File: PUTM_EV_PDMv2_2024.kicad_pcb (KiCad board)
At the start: 4 copper layers, 60 x 40 mm, 4 parts

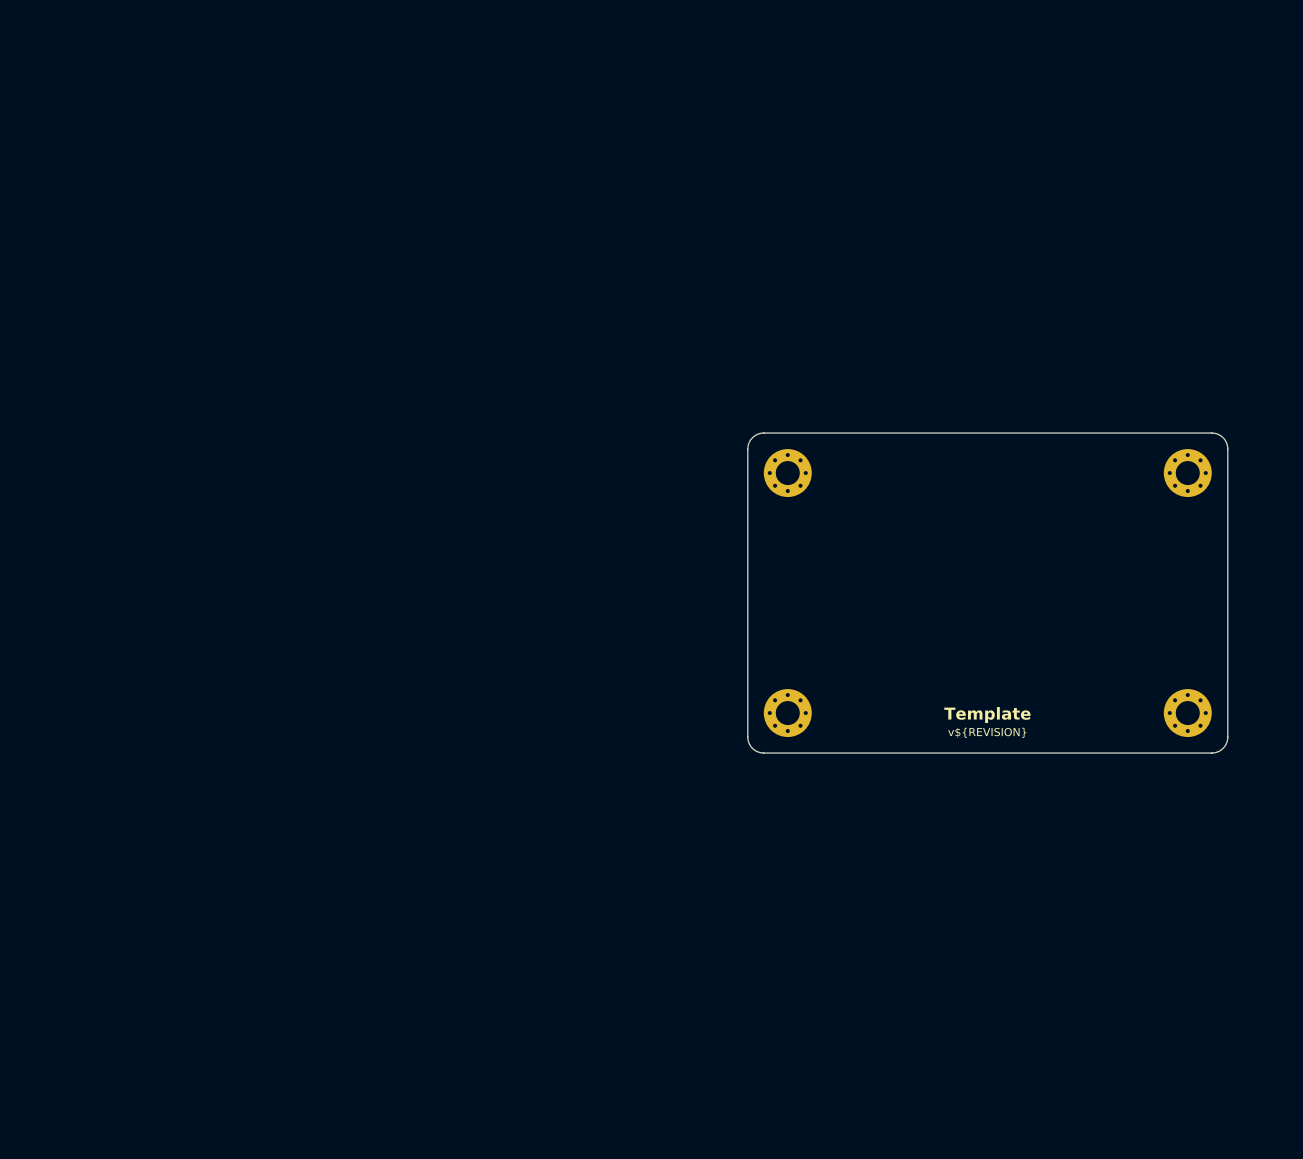
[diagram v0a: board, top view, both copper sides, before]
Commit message: Footprint changes + started PCB
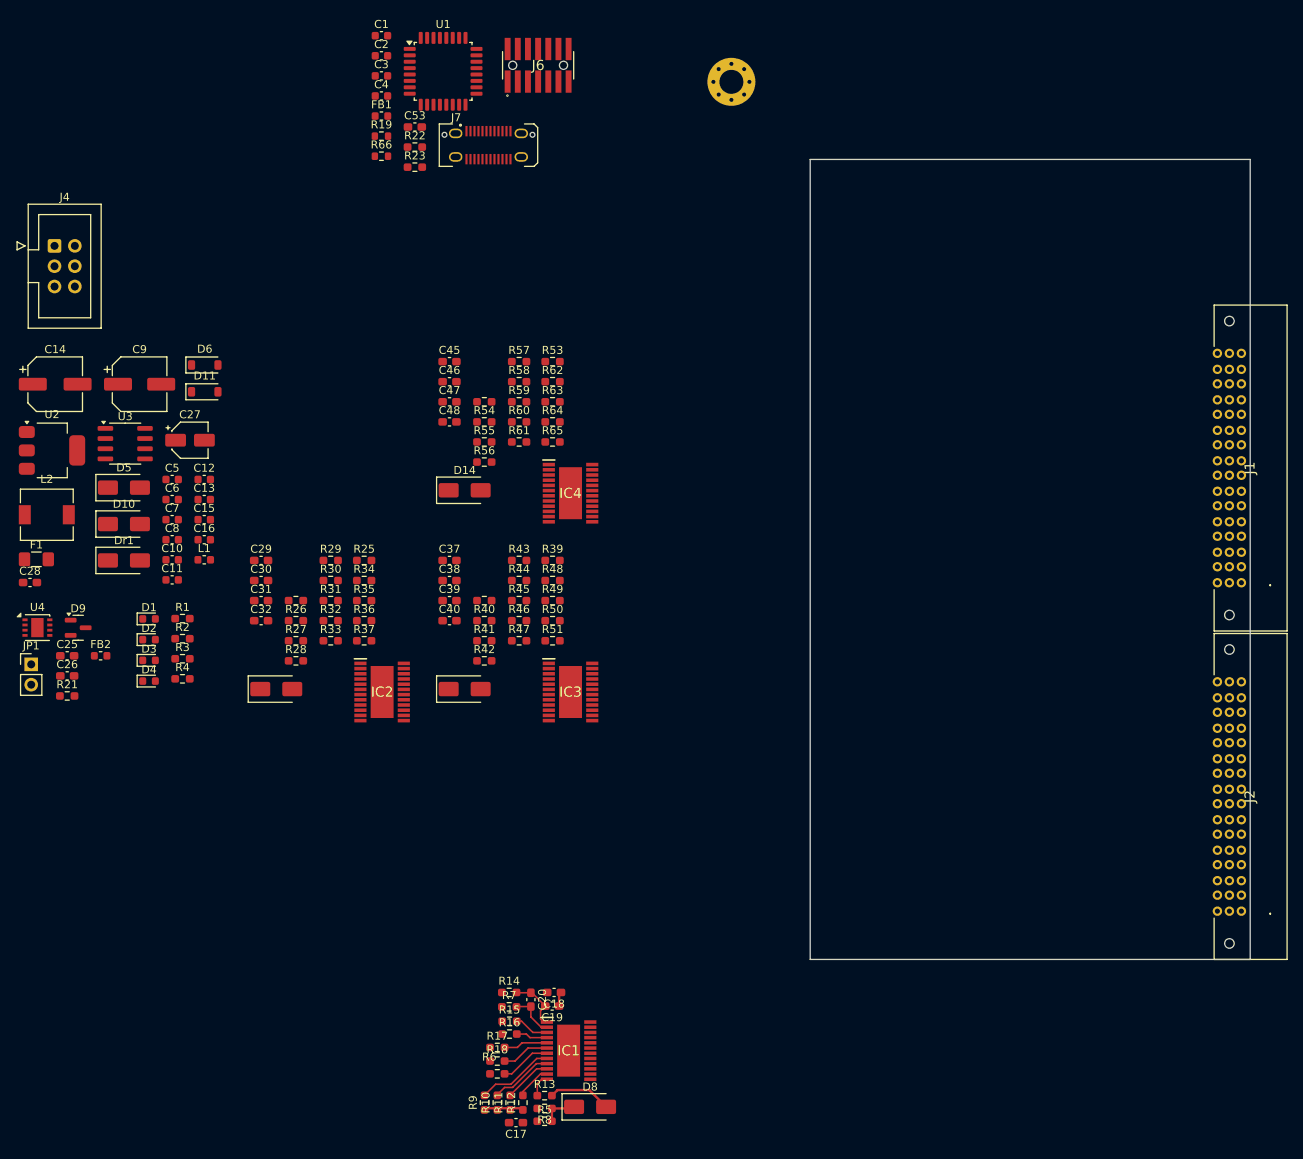
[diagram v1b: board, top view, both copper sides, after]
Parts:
- removed the REF** at (171.0, 81.0)
- removed the REF** at (121.0, 111.0)
- removed the REF** at (171.0, 111.0)
- added C1: 100n, Capacitor_SMD:C_0603_1608Metric, F.Cu at (70.2, 26.3)
- added C10: 100n, Capacitor_SMD:C_0603_1608Metric, F.Cu at (44.0, 91.8)
- added C11: 1u, Capacitor_SMD:C_0603_1608Metric, F.Cu at (44.0, 94.4)
- added C12: 10n, Capacitor_SMD:C_0603_1608Metric, F.Cu at (48.1, 81.8)
- added C13: 100n, Capacitor_SMD:C_0603_1608Metric, F.Cu at (48.1, 84.3)
- added C14: 68u, Capacitor_SMD:CP_Elec_6.3x5.4, F.Cu at (29.4, 69.9)
- added C15: 1u, Capacitor_SMD:C_0603_1608Metric, F.Cu at (48.1, 86.8)
- added C16: 100n, Capacitor_SMD:C_0603_1608Metric, F.Cu at (48.1, 89.3)
- added C17: 220p, Capacitor_SMD:C_0603_1608Metric_Pad1.08x0.95mm_HandSolder, F.Cu at (87.0, 162.2)
- added C18: 100n, Capacitor_SMD:C_0603_1608Metric_Pad1.08x0.95mm_HandSolder, F.Cu at (91.8, 145.9)
- added C19: 22n, Capacitor_SMD:C_0603_1608Metric_Pad1.08x0.95mm_HandSolder, F.Cu at (91.6, 147.6)
- added C2: 4.7u, Capacitor_SMD:C_0603_1608Metric, F.Cu at (70.2, 28.8)
- added C20: 470n, Capacitor_SMD:C_0603_1608Metric_Pad1.08x0.95mm_HandSolder, F.Cu at (88.9, 146.8)
- added C25: 100nF, Capacitor_SMD:C_0603_1608Metric_Pad1.08x0.95mm_HandSolder, F.Cu at (30.9, 103.8)
- added C26: 100nF, Capacitor_SMD:C_0603_1608Metric_Pad1.08x0.95mm_HandSolder, F.Cu at (30.9, 106.4)
- added C27: 22uF, Capacitor_SMD:CP_Elec_4x4.5, F.Cu at (46.3, 76.9)
- added C28: 1uF, Capacitor_SMD:C_0603_1608Metric_Pad1.08x0.95mm_HandSolder, F.Cu at (26.3, 94.7)
- added C29: 220p, Capacitor_SMD:C_0603_1608Metric_Pad1.08x0.95mm_HandSolder, F.Cu at (55.2, 91.9)
- added C3: 100n, Capacitor_SMD:C_0603_1608Metric, F.Cu at (70.2, 31.4)
- added C30: 100n, Capacitor_SMD:C_0603_1608Metric_Pad1.08x0.95mm_HandSolder, F.Cu at (55.2, 94.4)
- added C31: 22n, Capacitor_SMD:C_0603_1608Metric_Pad1.08x0.95mm_HandSolder, F.Cu at (55.2, 96.9)
- added C32: 470n, Capacitor_SMD:C_0603_1608Metric_Pad1.08x0.95mm_HandSolder, F.Cu at (55.2, 99.5)
- added C37: 220p, Capacitor_SMD:C_0603_1608Metric_Pad1.08x0.95mm_HandSolder, F.Cu at (78.7, 91.9)
- added C38: 100n, Capacitor_SMD:C_0603_1608Metric_Pad1.08x0.95mm_HandSolder, F.Cu at (78.7, 94.4)
- added C39: 22n, Capacitor_SMD:C_0603_1608Metric_Pad1.08x0.95mm_HandSolder, F.Cu at (78.7, 96.9)
- added C4: 4.7u, Capacitor_SMD:C_0603_1608Metric, F.Cu at (70.2, 33.9)
- added C40: 470n, Capacitor_SMD:C_0603_1608Metric_Pad1.08x0.95mm_HandSolder, F.Cu at (78.7, 99.5)
- added C45: 220p, Capacitor_SMD:C_0603_1608Metric_Pad1.08x0.95mm_HandSolder, F.Cu at (78.7, 67.1)
- added C46: 100n, Capacitor_SMD:C_0603_1608Metric_Pad1.08x0.95mm_HandSolder, F.Cu at (78.7, 69.6)
- added C47: 22n, Capacitor_SMD:C_0603_1608Metric_Pad1.08x0.95mm_HandSolder, F.Cu at (78.7, 72.1)
- added C48: 470n, Capacitor_SMD:C_0603_1608Metric_Pad1.08x0.95mm_HandSolder, F.Cu at (78.7, 74.6)
- added C5: 1u, Capacitor_SMD:C_0603_1608Metric, F.Cu at (44.0, 81.8)
- added C53: 10n, Capacitor_SMD:C_0603_1608Metric_Pad1.08x0.95mm_HandSolder, F.Cu at (74.4, 37.7)
- added C6: 10u, Capacitor_SMD:C_0603_1608Metric, F.Cu at (44.0, 84.3)
- added C7: 100n, Capacitor_SMD:C_0603_1608Metric, F.Cu at (44.0, 86.8)
- added C8: 100n, Capacitor_SMD:C_0603_1608Metric, F.Cu at (44.0, 89.3)
- added C9: 100u, Capacitor_SMD:CP_Elec_6.3x7.7, F.Cu at (40.0, 69.9)
- added D1: 150060SS75000, LED_SMD:LED_0603_1608Metric, F.Cu at (41.2, 99.2)
- added D10: 0.1/1A, Diode_SMD:D_SMA, F.Cu at (38.0, 87.4)
- added D11: 6V, Diode_SMD:D_SOD-123, F.Cu at (48.1, 70.8)
- added D12: D_Schottky, Diode_SMD:D_SMA, F.Cu at (57.1, 108.0)
- added D13: D_Schottky, Diode_SMD:D_SMA, F.Cu at (80.6, 108.0)
- added D14: D_Schottky, Diode_SMD:D_SMA, F.Cu at (80.6, 83.2)
- added D2: 150060SS75000, LED_SMD:LED_0603_1608Metric, F.Cu at (41.2, 101.8)
- added D3: 150060SS75000, LED_SMD:LED_0603_1608Metric, F.Cu at (41.2, 104.4)
- added D4: 150060SS75000, LED_SMD:LED_0603_1608Metric, F.Cu at (41.2, 107.0)
- added D5: SMAJ24CA-13-F, Diode_SMD:D_SMA, F.Cu at (38.0, 82.8)
- added D6: SS26FL, Diode_SMD:D_SOD-123, F.Cu at (48.1, 67.5)
- added D8: D_Schottky, Diode_SMD:D_SMA, F.Cu at (96.3, 160.2)
- added D9: PESD2CAN.215, Package_TO_SOT_SMD:SOT-23, F.Cu at (32.3, 100.3)
- added Dr1: SS34ALH, Diode_SMD:D_SMA, F.Cu at (38.0, 91.9)
- added F1: 5V/0.5A, Fuse:Fuse_1206_3216Metric_Pad1.42x1.75mm_HandSolder, F.Cu at (27.1, 91.8)
- added FB1: BLM18SP102SZ1D, Inductor_SMD:L_0603_1608Metric, F.Cu at (70.2, 36.4)
- added FB2: 60R@100MHz, Inductor_SMD:L_0603_1608Metric, F.Cu at (35.1, 103.8)
- added IC1: BTS722204ESAXUMA1, BTS722204ESAXUMA1:SOP65P600X115-25N, F.Cu at (93.6, 153.2)
- added IC2: BTS722204ESAXUMA1, BTS722204ESAXUMA1:SOP65P600X115-25N, F.Cu at (70.3, 108.4)
- added IC3: BTS722204ESAXUMA1, BTS722204ESAXUMA1:SOP65P600X115-25N, F.Cu at (93.8, 108.4)
- added IC4: BTS722204ESAXUMA1, BTS722204ESAXUMA1:SOP65P600X115-25N, F.Cu at (93.8, 83.5)
- added J1: UPT-08-01-01-L-RA, UPT-08-01.0-01-L-RA:UPT080101LRA, F.Cu at (177.7, 94.7)
- added J2: UPT-08-01-01-L-RA, UPT-08-01.0-01-L-RA:UPT080101LRA, F.Cu at (177.7, 135.8)
- added J4: Conn_01x06, Connector_IDC:IDC-Header_2x03_P2.54mm_Vertical, F.Cu at (29.3, 52.6)
- added J6: FTSH-107-01-L-DV-K-A, FTSH-107-01-L-DV-K-A:FTSH-107-XX-YYY-DV-K-A, F.Cu at (89.8, 30.0)
- added J7: USB_C_Receptacle_USB2.0_14P, Connector_USB:USB_C_Receptacle_JAE_DX07S024WJ3R400, F.Cu at (83.6, 40.0)
- added JP1: Jumper_2_Bridged, Connector_PinHeader_2.54mm:PinHeader_1x02_P2.54mm_Vertical, F.Cu at (26.4, 104.9)
- added L1: 300n, Inductor_SMD:L_0603_1608Metric, F.Cu at (48.1, 91.8)
- added L2: 47u, Inductor_SMD:L_6.3x6.3_H3, F.Cu at (28.4, 86.2)
- added R1: 150, Resistor_SMD:R_0603_1608Metric_Pad0.98x0.95mm_HandSolder, F.Cu at (45.3, 99.2)
- added R10: 10k, Resistor_SMD:R_0603_1608Metric_Pad0.98x0.95mm_HandSolder, F.Cu at (84.7, 159.7)
- added R11: 10k, Resistor_SMD:R_0603_1608Metric_Pad0.98x0.95mm_HandSolder, F.Cu at (86.3, 159.7)
- added R12: 10k, Resistor_SMD:R_0603_1608Metric_Pad0.98x0.95mm_HandSolder, F.Cu at (87.9, 159.7)
- added R13: 1.2k, Resistor_SMD:R_0603_1608Metric_Pad0.98x0.95mm_HandSolder, F.Cu at (90.6, 158.8)
- added R14: 47, Resistor_SMD:R_0603_1608Metric_Pad0.98x0.95mm_HandSolder, F.Cu at (86.2, 145.9)
- added R15: 330, Resistor_SMD:R_0603_1608Metric_Pad0.98x0.95mm_HandSolder, F.Cu at (86.2, 149.5)
- added R16: 330, Resistor_SMD:R_0603_1608Metric_Pad0.98x0.95mm_HandSolder, F.Cu at (86.2, 151.1)
- added R17: 330, Resistor_SMD:R_0603_1608Metric_Pad0.98x0.95mm_HandSolder, F.Cu at (84.7, 152.8)
- added R18: 330, Resistor_SMD:R_0603_1608Metric_Pad0.98x0.95mm_HandSolder, F.Cu at (84.7, 154.5)
- added R19: 100k, Resistor_SMD:R_0603_1608Metric, F.Cu at (70.2, 38.9)
- added R2: 150, Resistor_SMD:R_0603_1608Metric_Pad0.98x0.95mm_HandSolder, F.Cu at (45.3, 101.7)
- added R21: 120, Resistor_SMD:R_0603_1608Metric_Pad0.98x0.95mm_HandSolder, F.Cu at (30.9, 108.9)
- added R22: 5.1k, Resistor_SMD:R_0603_1608Metric_Pad0.98x0.95mm_HandSolder, F.Cu at (74.4, 40.3)
- added R23: 5.1k, Resistor_SMD:R_0603_1608Metric_Pad0.98x0.95mm_HandSolder, F.Cu at (74.4, 42.8)
- added R24: 4.7k, Resistor_SMD:R_0603_1608Metric_Pad0.98x0.95mm_HandSolder, F.Cu at (59.5, 96.9)
- added R25: 4.7k, Resistor_SMD:R_0603_1608Metric_Pad0.98x0.95mm_HandSolder, F.Cu at (68.0, 91.9)
- added R26: 470, Resistor_SMD:R_0603_1608Metric_Pad0.98x0.95mm_HandSolder, F.Cu at (59.5, 99.5)
- added R27: 4.7k, Resistor_SMD:R_0603_1608Metric_Pad0.98x0.95mm_HandSolder, F.Cu at (59.5, 102.0)
- added R28: 10k, Resistor_SMD:R_0603_1608Metric_Pad0.98x0.95mm_HandSolder, F.Cu at (59.5, 104.5)
- added R29: 10k, Resistor_SMD:R_0603_1608Metric_Pad0.98x0.95mm_HandSolder, F.Cu at (63.9, 91.9)
- added R3: 150, Resistor_SMD:R_0603_1608Metric_Pad0.98x0.95mm_HandSolder, F.Cu at (45.3, 104.2)
- added R30: 10k, Resistor_SMD:R_0603_1608Metric_Pad0.98x0.95mm_HandSolder, F.Cu at (63.9, 94.4)
- added R31: 10k, Resistor_SMD:R_0603_1608Metric_Pad0.98x0.95mm_HandSolder, F.Cu at (63.9, 96.9)
- added R32: 1.2k, Resistor_SMD:R_0603_1608Metric_Pad0.98x0.95mm_HandSolder, F.Cu at (63.9, 99.5)
- added R33: 47, Resistor_SMD:R_0603_1608Metric_Pad0.98x0.95mm_HandSolder, F.Cu at (63.9, 102.0)
- added R34: 330, Resistor_SMD:R_0603_1608Metric_Pad0.98x0.95mm_HandSolder, F.Cu at (68.0, 94.4)
- added R35: 330, Resistor_SMD:R_0603_1608Metric_Pad0.98x0.95mm_HandSolder, F.Cu at (68.0, 96.9)
- added R36: 330, Resistor_SMD:R_0603_1608Metric_Pad0.98x0.95mm_HandSolder, F.Cu at (68.0, 99.5)
- added R37: 330, Resistor_SMD:R_0603_1608Metric_Pad0.98x0.95mm_HandSolder, F.Cu at (68.0, 102.0)
- added R38: 4.7k, Resistor_SMD:R_0603_1608Metric_Pad0.98x0.95mm_HandSolder, F.Cu at (83.1, 96.9)
- added R39: 4.7k, Resistor_SMD:R_0603_1608Metric_Pad0.98x0.95mm_HandSolder, F.Cu at (91.6, 91.9)
- added R4: 150, Resistor_SMD:R_0603_1608Metric_Pad0.98x0.95mm_HandSolder, F.Cu at (45.3, 106.7)
- added R40: 470, Resistor_SMD:R_0603_1608Metric_Pad0.98x0.95mm_HandSolder, F.Cu at (83.1, 99.5)
- added R41: 4.7k, Resistor_SMD:R_0603_1608Metric_Pad0.98x0.95mm_HandSolder, F.Cu at (83.1, 102.0)
- added R42: 10k, Resistor_SMD:R_0603_1608Metric_Pad0.98x0.95mm_HandSolder, F.Cu at (83.1, 104.5)
- added R43: 10k, Resistor_SMD:R_0603_1608Metric_Pad0.98x0.95mm_HandSolder, F.Cu at (87.4, 91.9)
- added R44: 10k, Resistor_SMD:R_0603_1608Metric_Pad0.98x0.95mm_HandSolder, F.Cu at (87.4, 94.4)
- added R45: 10k, Resistor_SMD:R_0603_1608Metric_Pad0.98x0.95mm_HandSolder, F.Cu at (87.4, 96.9)
- added R46: 1.2k, Resistor_SMD:R_0603_1608Metric_Pad0.98x0.95mm_HandSolder, F.Cu at (87.4, 99.5)
- added R47: 47, Resistor_SMD:R_0603_1608Metric_Pad0.98x0.95mm_HandSolder, F.Cu at (87.4, 102.0)
- added R48: 330, Resistor_SMD:R_0603_1608Metric_Pad0.98x0.95mm_HandSolder, F.Cu at (91.6, 94.4)
- added R49: 330, Resistor_SMD:R_0603_1608Metric_Pad0.98x0.95mm_HandSolder, F.Cu at (91.6, 96.9)
- added R5: 4.7k, Resistor_SMD:R_0603_1608Metric_Pad0.98x0.95mm_HandSolder, F.Cu at (90.6, 162.0)
- added R50: 330, Resistor_SMD:R_0603_1608Metric_Pad0.98x0.95mm_HandSolder, F.Cu at (91.6, 99.5)
- added R51: 330, Resistor_SMD:R_0603_1608Metric_Pad0.98x0.95mm_HandSolder, F.Cu at (91.6, 102.0)
- added R52: 4.7k, Resistor_SMD:R_0603_1608Metric_Pad0.98x0.95mm_HandSolder, F.Cu at (83.1, 72.1)
- added R53: 4.7k, Resistor_SMD:R_0603_1608Metric_Pad0.98x0.95mm_HandSolder, F.Cu at (91.6, 67.1)
- added R54: 470, Resistor_SMD:R_0603_1608Metric_Pad0.98x0.95mm_HandSolder, F.Cu at (83.1, 74.6)
- added R55: 4.7k, Resistor_SMD:R_0603_1608Metric_Pad0.98x0.95mm_HandSolder, F.Cu at (83.1, 77.1)
- added R56: 10k, Resistor_SMD:R_0603_1608Metric_Pad0.98x0.95mm_HandSolder, F.Cu at (83.1, 79.6)
- added R57: 10k, Resistor_SMD:R_0603_1608Metric_Pad0.98x0.95mm_HandSolder, F.Cu at (87.4, 67.1)
- added R58: 10k, Resistor_SMD:R_0603_1608Metric_Pad0.98x0.95mm_HandSolder, F.Cu at (87.4, 69.6)
- added R59: 10k, Resistor_SMD:R_0603_1608Metric_Pad0.98x0.95mm_HandSolder, F.Cu at (87.4, 72.1)
- added R6: 4.7k, Resistor_SMD:R_0603_1608Metric_Pad0.98x0.95mm_HandSolder, F.Cu at (84.7, 156.1)
- added R60: 1.2k, Resistor_SMD:R_0603_1608Metric_Pad0.98x0.95mm_HandSolder, F.Cu at (87.4, 74.6)
- added R61: 47, Resistor_SMD:R_0603_1608Metric_Pad0.98x0.95mm_HandSolder, F.Cu at (87.4, 77.1)
- added R62: 330, Resistor_SMD:R_0603_1608Metric_Pad0.98x0.95mm_HandSolder, F.Cu at (91.6, 69.6)
- added R63: 330, Resistor_SMD:R_0603_1608Metric_Pad0.98x0.95mm_HandSolder, F.Cu at (91.6, 72.1)
- added R64: 330, Resistor_SMD:R_0603_1608Metric_Pad0.98x0.95mm_HandSolder, F.Cu at (91.6, 74.6)
- added R65: 330, Resistor_SMD:R_0603_1608Metric_Pad0.98x0.95mm_HandSolder, F.Cu at (91.6, 77.1)
- added R66: 100k, Resistor_SMD:R_0603_1608Metric, F.Cu at (70.2, 41.4)
- added R7: 470, Resistor_SMD:R_0603_1608Metric_Pad0.98x0.95mm_HandSolder, F.Cu at (86.2, 147.7)
- added R8: 4.7k, Resistor_SMD:R_0603_1608Metric_Pad0.98x0.95mm_HandSolder, F.Cu at (90.6, 160.4)
- added R9: 10k, Resistor_SMD:R_0603_1608Metric_Pad0.98x0.95mm_HandSolder, F.Cu at (83.1, 159.7)
- added U1: STM32G0C1KCTxN, Package_QFP:LQFP-32_7x7mm_P0.8mm, F.Cu at (77.9, 30.8)
- added U2: LD1117S33TR_SOT223, Package_TO_SOT_SMD:SOT-223-3_TabPin2, F.Cu at (29.0, 78.2)
- added U3: LM2675M-5.0/NOPB, Package_SO:SOIC-8_3.9x4.9mm_P1.27mm, F.Cu at (38.2, 77.3)
- added U4: MCP2542FDxMF, Package_DFN_QFN:DFN-8-1EP_3x3mm_P0.65mm_EP1.55x2.4mm, F.Cu at (27.2, 100.3)
- moved REF** 49.4 mm to (114.0, 32.1)
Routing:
- net GND: track 0.00 -> 12.7 mm
- net /Controllers/IC_1/IN0: track 0.00 -> 9.71 mm
- net /Controllers/IC_1/IN1: track 0.00 -> 7.89 mm
- net Net-(IC1-GND_1): track 0.00 -> 7.12 mm
- net Net-(IC1-LHI): track 0.00 -> 6.35 mm
- net /Controllers/IC_1/IN2: track 0.00 -> 5.97 mm
- net Net-(IC1-CSN): track 0.00 -> 5.96 mm
- net Net-(IC1-VDD): track 0.00 -> 5.65 mm
- net Net-(IC1-SCLK): track 0.00 -> 5.53 mm
- net Net-(D8-K): track 0.00 -> 4.46 mm
- net /Controllers/IC_1/IN3: track 0.00 -> 4.38 mm
- net Net-(IC1-SO): track 0.00 -> 4.34 mm
- net Net-(IC1-SI): track 0.00 -> 3.95 mm
- net Net-(IC1-IS): track 0.00 -> 2.93 mm
- net +BATT: track 0.00 -> 1.80 mm
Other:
- board size 60 x 40 mm -> 55 x 100 mm
- board text removed: "Template"
- board text removed: "v${REVISION}"

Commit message: Layout done
Added layout
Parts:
- removed D12, D13, D14: D_Schottky, Diode_SMD:D_SMA
- removed the D8 at (96.3, 160.2)
- removed FB1: BLM18SP102SZ1D, Inductor_SMD:L_0603_1608Metric
- removed J2: UPT-08-01-01-L-RA, UPT-08-01.0-01-L-RA:UPT080101LRA
- removed R66: 100k, Resistor_SMD:R_0603_1608Metric
- added D16: SKL34, SKL34:SODFL3718X140N, F.Cu at (160.1, 138.2)
- added D17: SKL34, SKL34:SODFL3718X140N, F.Cu at (160.2, 121.0)
- added D18: SKL34, SKL34:SODFL3718X140N, F.Cu at (160.2, 103.7)
- added D19: SKL34, SKL34:SODFL3718X140N, F.Cu at (160.3, 86.8)
- added J5: UMPT-08-01-L-RA-WT-P-TR, UMPT-08-01-L-RA-WT-P-TR:SAMTEC_UMPT-08-01-L-RA-WT-P-TR, F.Cu at (175.9, 86.8)
- added J8: UMPT-08-01-L-RA-WT-P-TR, UMPT-08-01-L-RA-WT-P-TR:SAMTEC_UMPT-08-01-L-RA-WT-P-TR, F.Cu at (175.9, 123.8)
- added R20: 0, Resistor_SMD:R_0603_1608Metric_Pad0.98x0.95mm_HandSolder, F.Cu at (134.7, 104.7)
- added REF**: MountingHole_3mm_Pad_Via, MountingHole:MountingHole_3mm_Pad_Via, F.Cu at (174.6, 105.2)
- added REF**: MountingHole_3mm_Pad_Via, MountingHole:MountingHole_3mm_Pad_Via, F.Cu at (125.2, 138.0)
- C25, C26: value 100nF -> 100n
- C27: value 22uF -> 22u
- C28: value 1uF -> 1u
- J1: value UPT-08-01-01-L-RA -> 74650073R; footprint UPT-08-01.0-01-L-RA:UPT080101LRA -> Redcube conn:74650073R
- moved D8 132.7 mm to (168.7, 68.8)
- moved D5 128.6 mm to (164.6, 60.2), turned to -90 degrees
- moved L2 122.9 mm to (148.3, 59.1), turned to 180 degrees
- moved C6 119.5 mm to (162.7, 69.8), turned to 90 degrees
- moved C9 118.7 mm to (158.3, 60.2), turned to 90 degrees
- moved C5 117.5 mm to (160.9, 69.8), turned to 90 degrees
- moved C8 116.7 mm to (159.1, 69.8), turned to 90 degrees
- moved J4 116.2 mm to (124.5, 119.4)
- moved L1 114.6 mm to (160.0, 67.4), turned to 180 degrees
- moved C7 114.5 mm to (157.3, 69.8), turned to 90 degrees
- moved U3 110.5 mm to (148.2, 67.5)
- moved U2 110.4 mm to (139.4, 75.0), turned to 180 degrees
- moved D6 106.1 mm to (154.2, 66.9), turned to -90 degrees
- moved F1 106.0 mm to (132.7, 81.8), turned to 180 degrees
- moved D4 105.5 mm to (141.9, 138.3), turned to 90 degrees
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- renumbered Dr1 to D8
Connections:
- C53 pad 1: GND -> Net-(J7-SHIELD)
- J6 pad 12: /RST -> /NRST
- J7 pad S1: GND -> Net-(J7-SHIELD)
- REF** pad 1: (no net) -> GND
- U1 pad 17: /LED3 -> /LED4
- U1 pad 18: /LED2 -> /LED3
- U1 pad 19: /LED1 -> /LED2
- U1 pad 21: /LED4 -> /LED1
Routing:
- net +3.3V: track 0.00 -> 135.0 mm, vias 0 -> 27
- net /SPI1_NSS: track 0.00 -> 65.4 mm, vias 0 -> 6
- net /SPI1_SCK: track 0.00 -> 60.8 mm, vias 0 -> 5
- net /LHI_1: track 0.00 -> 51.6 mm, vias 0 -> 2
- net /LHI_2: track 0.00 -> 51.5 mm, vias 0 -> 2
- net /FUSE1_IS: track 0.00 -> 48.8 mm
- net /LED1: track 0.00 -> 48.3 mm, vias 0 -> 2
- net /LED2: track 0.00 -> 48.2 mm, vias 0 -> 2
- net /LED3: track 0.00 -> 46.8 mm, vias 0 -> 2
- net /LED4: track 0.00 -> 46.7 mm, vias 0 -> 2
- net /SPI1_MOSI: track 0.00 -> 43.7 mm, vias 0 -> 2
- net +5V: track 0.00 -> 37.0 mm
- net /SWDIO: track 0.00 -> 35.9 mm, vias 0 -> 2
- net /FUSE2_IS: track 0.00 -> 32.1 mm
- net /SWCLK: track 0.00 -> 29.6 mm, vias 0 -> 2
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- added copper zone on F.Cu, net +3.3V
- added copper zone on In1.Cu, net +3.3V
- added copper zone on F.Cu, net +5V
- added copper zone on B.Cu, net +BATT
- added copper zone on F.Cu, net +BATT
- added copper zone on F.Cu, net /Power/CB
- added copper zone on F.Cu, net /Power/SW_L
- added copper zone on F.Cu, net /Power/VIN_L
- added copper zone on F.Cu, net /Power/VIN_SW_REG
- added copper zone on B.Cu, net GND
- added copper zone on F.Cu, net GND
- added copper zone on In1.Cu, net GND
- added copper zone on In2.Cu, net GND
- added copper zone on F.Cu, net Net-(D10-K)
- added copper zone on F.Cu, net OUT1_0
- added copper zone on In1.Cu, net OUT1_0
- added copper zone on In2.Cu, net OUT1_0
- added copper zone on F.Cu, net OUT1_1
- added copper zone on In1.Cu, net OUT1_1
- added copper zone on In2.Cu, net OUT1_1
- added copper zone on F.Cu, net OUT1_2
- added copper zone on In1.Cu, net OUT1_2
- added copper zone on In2.Cu, net OUT1_2
- added copper zone on F.Cu, net OUT1_3
- added copper zone on In1.Cu, net OUT1_3
- added copper zone on In2.Cu, net OUT1_3
- added copper zone on F.Cu, net OUT2_0
- added copper zone on In1.Cu, net OUT2_0
- added copper zone on In2.Cu, net OUT2_0
- added copper zone on F.Cu, net OUT2_1
- added copper zone on In1.Cu, net OUT2_1
- added copper zone on In2.Cu, net OUT2_1
- added copper zone on F.Cu, net OUT2_2
- added copper zone on In1.Cu, net OUT2_2
- added copper zone on In2.Cu, net OUT2_2
- added copper zone on F.Cu, net OUT2_3
- added copper zone on In1.Cu, net OUT2_3
- added copper zone on In2.Cu, net OUT2_3
- added copper zone on F.Cu, net OUT3_0
- added copper zone on In1.Cu, net OUT3_0
- added copper zone on In2.Cu, net OUT3_0
- added copper zone on F.Cu, net OUT3_1
- added copper zone on In1.Cu, net OUT3_1
- added copper zone on In2.Cu, net OUT3_1
- added copper zone on F.Cu, net OUT3_2
- added copper zone on In1.Cu, net OUT3_2
- added copper zone on In2.Cu, net OUT3_2
- added copper zone on F.Cu, net OUT3_3
- added copper zone on In1.Cu, net OUT3_3
- added copper zone on In2.Cu, net OUT3_3
- added copper zone on F.Cu, net OUT4_0
- added copper zone on In1.Cu, net OUT4_0
- added copper zone on In2.Cu, net OUT4_0
- added copper zone on F.Cu, net OUT4_1
- added copper zone on In1.Cu, net OUT4_1
- added copper zone on In2.Cu, net OUT4_1
- added copper zone on F.Cu, net OUT4_2
- added copper zone on In1.Cu, net OUT4_2
- added copper zone on In2.Cu, net OUT4_2
- added copper zone on F.Cu, net OUT4_3
- added copper zone on In1.Cu, net OUT4_3
- added copper zone on In2.Cu, net OUT4_3
- added copper zone on F.Cu, net VBUS
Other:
- board size 55 x 100 mm -> 58 x 87.3 mm
